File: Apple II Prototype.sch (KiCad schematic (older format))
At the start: 1 part

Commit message: First layout draft
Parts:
- added J1: Breakout, Breakout:Breakout, symbol Breakout
- added P1, P2, P3, P36, P37, P38, P4, P5, P6, P7, P8: Prototype_26, Prototype:prototype_26, symbol Prototype_26
- added P10, P11, P12, P13, P14, P15, P16, P17, P18, P19, P20, P21, P22, P23, P24, P25, P26, P27, P28, P29, P30, P31, P32, P33, P34, P35, P9: Prototype_23, Prototype:prototype_23, symbol Prototype_23
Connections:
- net ~I/O_SEL: now reaches BUS1.1 (~I/O_SEL)
- net ~I/O_SEL: now also J1.1 (Pin_1)
- net A8: now reaches BUS1.10 (A8)
- net A8: now also J1.10 (Pin_10)
- net A9: now reaches BUS1.11 (A9)
- net A9: now also J1.11 (Pin_11)
- net A10: now reaches BUS1.12 (A10)
- net A10: now also J1.12 (Pin_12)
- net A11: now reaches BUS1.13 (A11)
- net A11: now also J1.13 (Pin_13)
- net A12: now reaches BUS1.14 (A12)
- net A12: now also J1.14 (Pin_14)
- net A13: now reaches BUS1.15 (A13)
- net A13: now also J1.15 (Pin_15)
- net A14: now reaches BUS1.16 (A14)
- net A14: now also J1.16 (Pin_16)
- net A15: now reaches BUS1.17 (A15)
- net A15: now also J1.17 (Pin_17)
- net R/~W: now reaches BUS1.18 (R/~W)
- net R/~W: now also J1.18 (Pin_18)
- net A0: now reaches BUS1.2 (A0)
- net A0: now also J1.2 (Pin_2)
- net ~STROBE: now reaches BUS1.20 (~STROBE)
- net ~STROBE: now also J1.20 (Pin_20)
- net RDY: now reaches BUS1.21 (RDY)
- net RDY: now also J1.21 (Pin_21)
- net ~DMA: now reaches BUS1.22 (~DMA)
- net ~DMA: now also J1.22 (Pin_22)
- net INT_OUT: now reaches BUS1.23 (INT_OUT)
- net INT_OUT: now also J1.23 (Pin_23)
- net DMA_OUT: now reaches BUS1.24 (DMA_OUT)
- net DMA_OUT: now also J1.24 (Pin_24)
- net +5V: now reaches BUS1.25 (+5V)
- net +5V: now also J1.25 (Pin_25)
- net GND: now reaches BUS1.26 (GND)
- net GND: now also J1.26 (Pin_26)
- net DMA_IN: now reaches BUS1.27 (DMA_IN)
- net DMA_IN: now also J1.27 (Pin_27)
- net INT_IN: now reaches BUS1.28 (INT_IN)
- net INT_IN: now also J1.28 (Pin_28)
- net ~NMI: now reaches BUS1.29 (~NMI)
- net ~NMI: now also J1.29 (Pin_29)
- net A1: now reaches BUS1.3 (A1)
- net A1: now also J1.3 (Pin_3)
- net ~IRQ: now reaches BUS1.30 (~IRQ)
- net ~IRQ: now also J1.30 (Pin_30)
- net ~RES: now reaches BUS1.31 (~RES)
- net ~RES: now also J1.31 (Pin_31)
- net ~INH: now reaches BUS1.32 (~INH)
- net ~INH: now also J1.32 (Pin_32)
- net -12V: now reaches BUS1.33 (-12V)
- net -12V: now also J1.33 (Pin_33)
- net -5V: now reaches BUS1.34 (-5V)
- net -5V: now also J1.34 (Pin_34)
- net 7M: now reaches BUS1.36 (7M)
- net 7M: now also J1.36 (Pin_36)
- net Q3: now reaches BUS1.37 (Q3)
- net Q3: now also J1.37 (Pin_37)
- net Phi1: now reaches BUS1.38 (ø1)
- net Phi1: now also J1.38 (Pin_38)
- net ~M2SEL: now reaches BUS1.39 (~M2SEL)
- net ~M2SEL: now also J1.39 (Pin_39)
- net A2: now reaches BUS1.4 (A2)
- net A2: now also J1.4 (Pin_4)
- net Phi0: now reaches BUS1.40 (ø0)
- net Phi0: now also J1.40 (Pin_40)
- net ~DEVSEL: now reaches BUS1.41 (~DEVSEL)
- net ~DEVSEL: now also J1.41 (Pin_41)
- net D7: now reaches BUS1.42 (D7)
- net D7: now also J1.42 (Pin_42)
- net D6: now reaches BUS1.43 (D6)
- net D6: now also J1.43 (Pin_43)
- net D5: now reaches BUS1.44 (D5)
- net D5: now also J1.44 (Pin_44)
- net D4: now reaches BUS1.45 (D4)
- net D4: now also J1.45 (Pin_45)
- net D3: now reaches BUS1.46 (D3)
- net D3: now also J1.46 (Pin_46)
- net D2: now reaches BUS1.47 (D2)
- net D2: now also J1.47 (Pin_47)
- net D1: now reaches BUS1.48 (D1)
- net D1: now also J1.48 (Pin_48)
- net D0: now reaches BUS1.49 (D0)
- net D0: now also J1.49 (Pin_49)
- net A3: now reaches BUS1.5 (A3)
- net A3: now also J1.5 (Pin_5)
- net +12V: now reaches BUS1.50 (+12V)
- net +12V: now also J1.50 (Pin_50)
- net A4: now reaches BUS1.6 (A4)
- net A4: now also J1.6 (Pin_6)
- net A5: now reaches BUS1.7 (A5)
- net A5: now also J1.7 (Pin_7)
- net A6: now reaches BUS1.8 (A6)
- net A6: now also J1.8 (Pin_8)
- net A7: now reaches BUS1.9 (A7)
- net A7: now also J1.9 (Pin_9)
- no-connect marks 0 -> 2

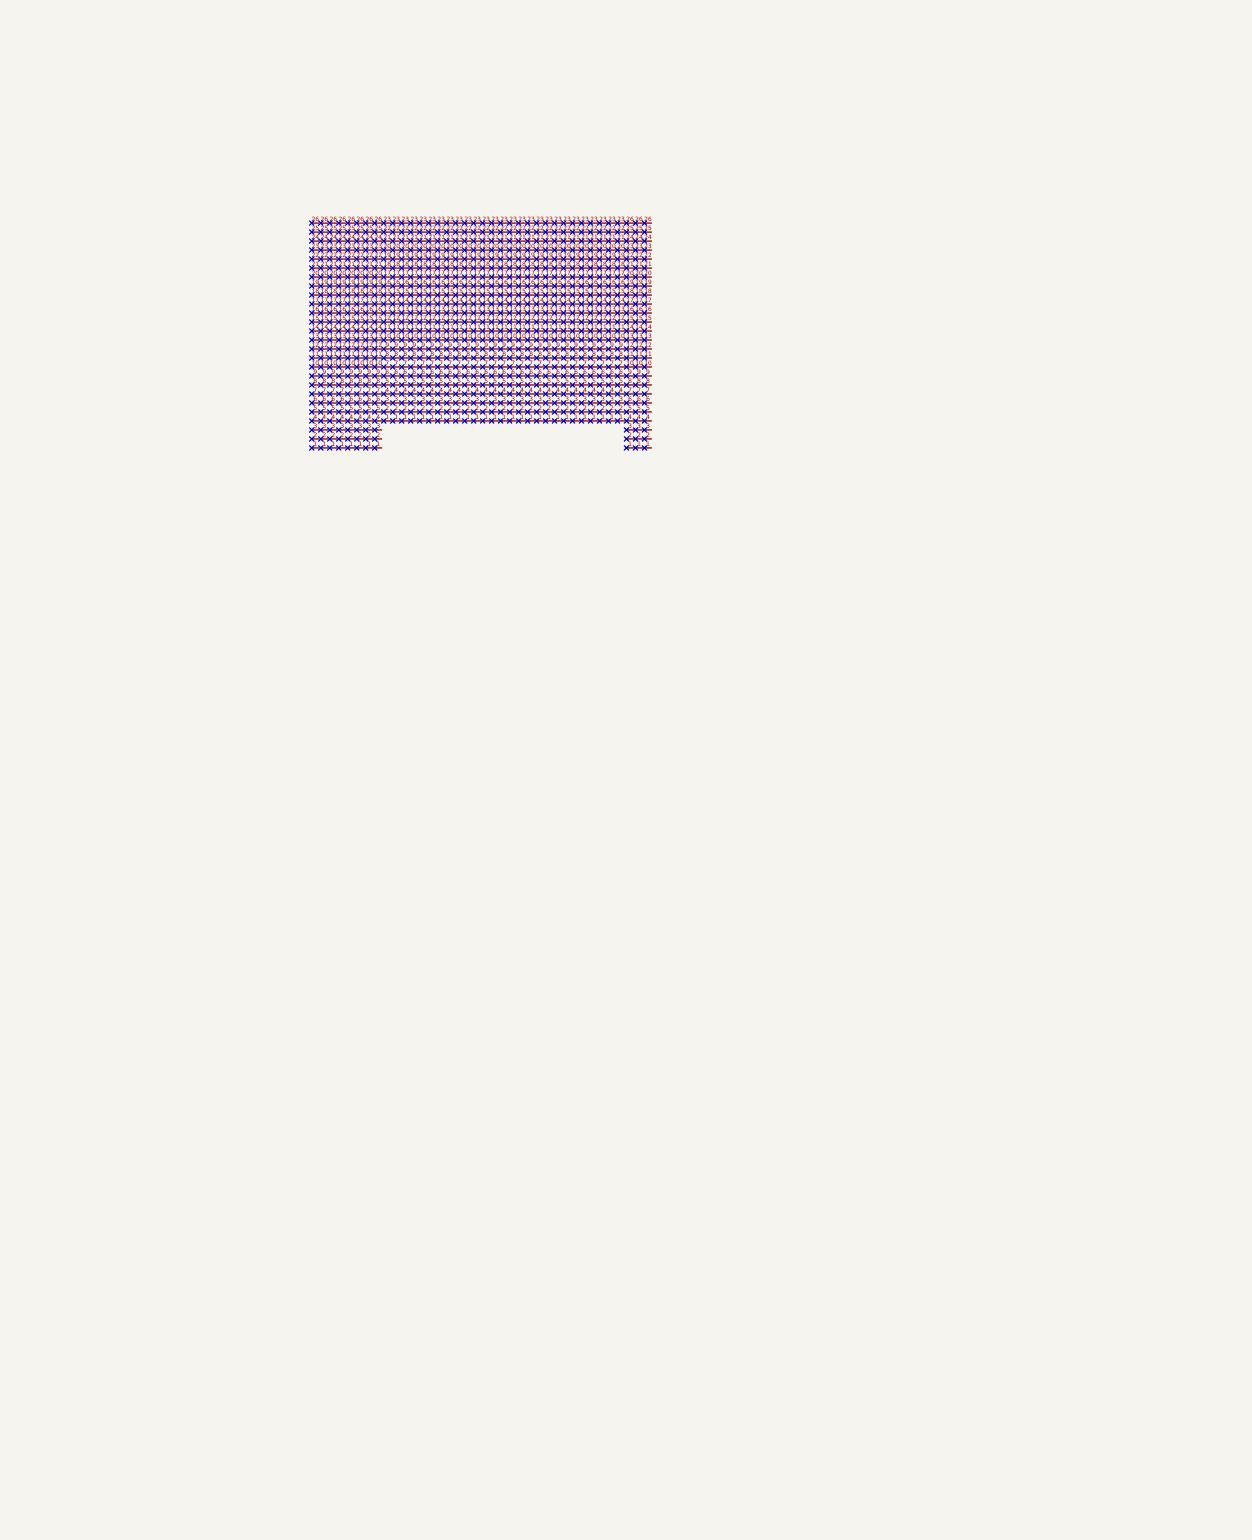
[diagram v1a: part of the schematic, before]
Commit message: Added source notices to schematic
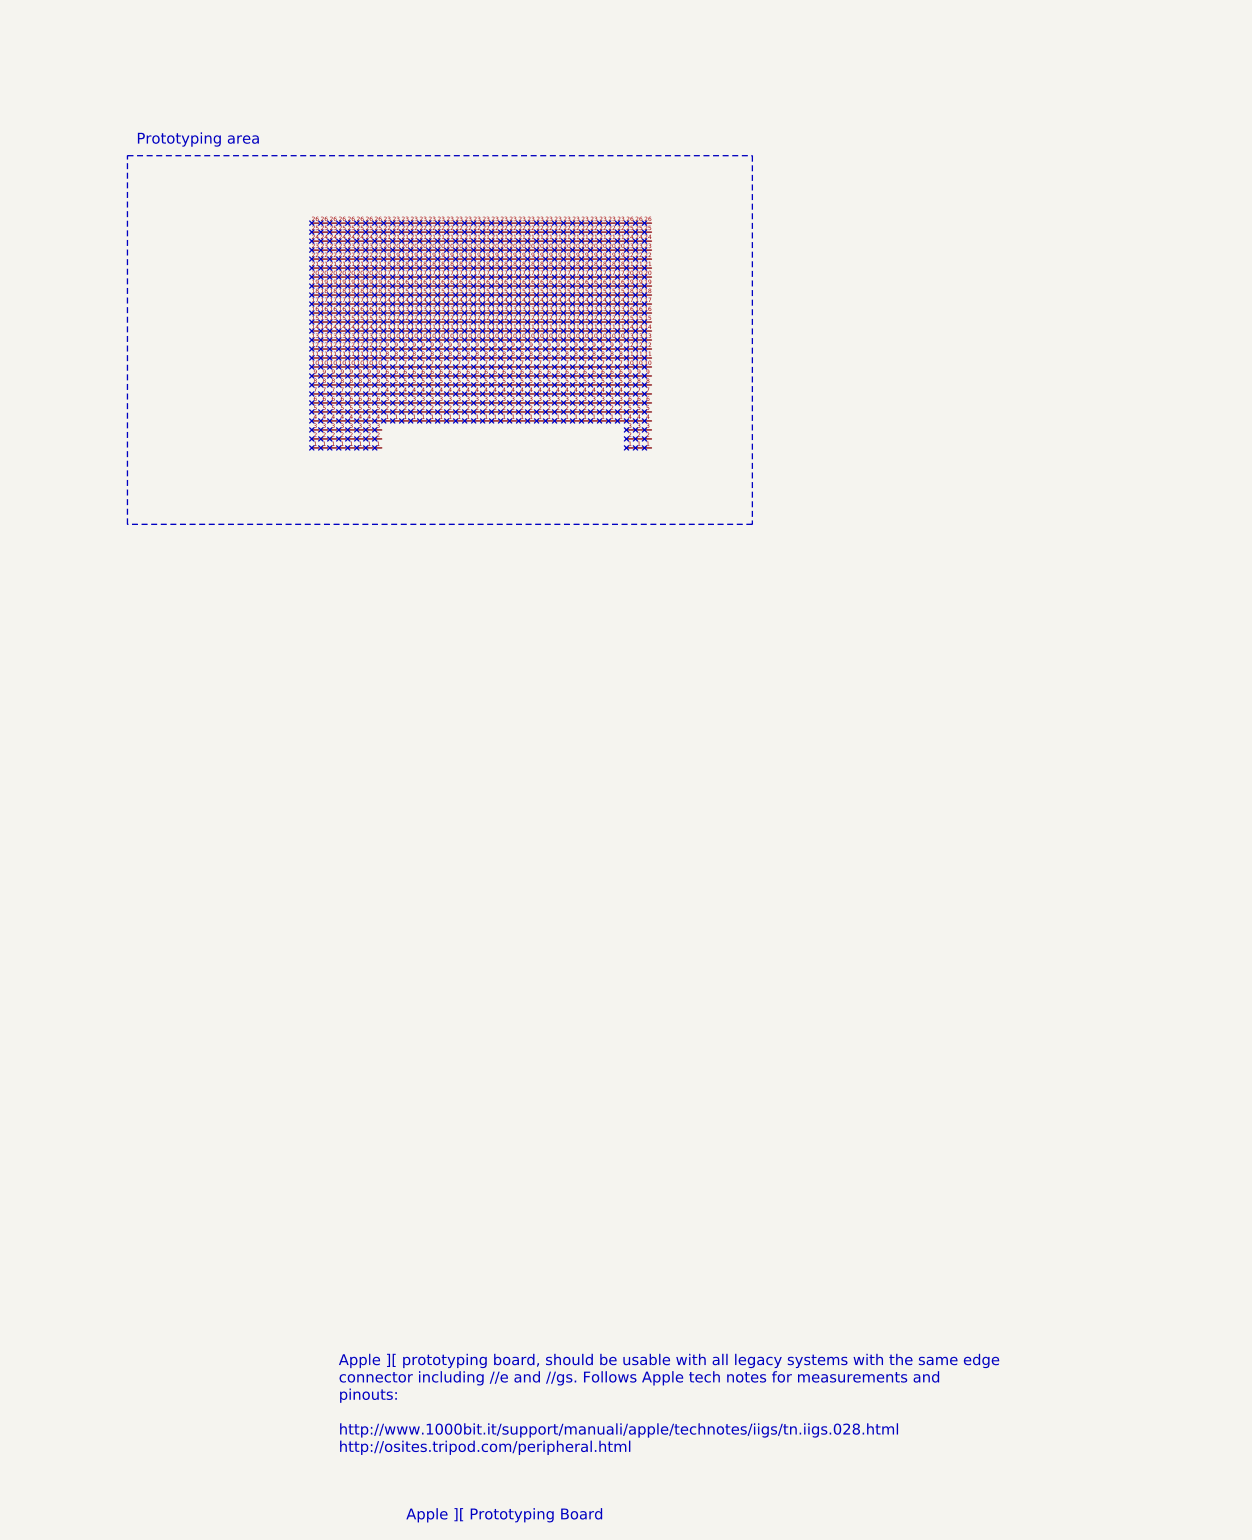
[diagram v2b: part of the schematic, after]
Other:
- note added: "Apple ][ Prototyping Board"
- note added: "Apple ][ prototyping board, should be usable with all legacy systems with the same edge\nconnector including //e and //gs. Follows Apple tech notes for measurements and\npinouts:\n\nhttp://www.1000bit.it/support/manuali/apple/technotes/iigs/tn.iigs.028.html\nhttp://osites.tripod.com/peripheral.html"
- note added: "Prototyping area"
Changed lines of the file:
@@
 	-1   0    0    1
 $EndComp
+Text Notes 12200 10925 0    60   ~ 0
+Apple ][ Prototyping Board
+Text Notes 11825 10550 0    60   ~ 0
+Apple ][ prototyping board, should be usable with all legacy systems with the same edge\nconnector including //e and //gs. Follows Apple tech notes for measurements and\npinouts:\n\nhttp://www.1000bit.it/support/manuali/apple/technotes/iigs/tn.iigs.028.html\nhttp://osites.tripod.com/peripheral.html
+Wire Notes Line
+	10650 3325 14125 3325
+Wire Notes Line
+	14125 3325 14125 5375
+Wire Notes Line
+	14125 5375 10650 5375
+Wire Notes Line
+	10650 5375 10650 3325
+Text Notes 10700 3275 0    60   ~ 0
+Prototyping area
 $EndSCHEMATC
